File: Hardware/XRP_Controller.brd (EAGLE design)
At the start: 63.5 x 54 mm, 212 parts, among them J1 POWER_JACKPOWER_JACK_SLOT, J12 Vertical Qwiic Connector, J13 Vertical Qwiic Connector, J14 Vertical Qwiic Connector, J3 JST_6_PIN_VERTICAL, J4 JST_6_PIN_VERTICAL, J5 JST_6_PIN_VERTICAL, J6 JST_6_PIN_VERTICAL, J9 Vertical Qwiic Connector, Q3 20V/4.2A/52mΩ/1.4W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

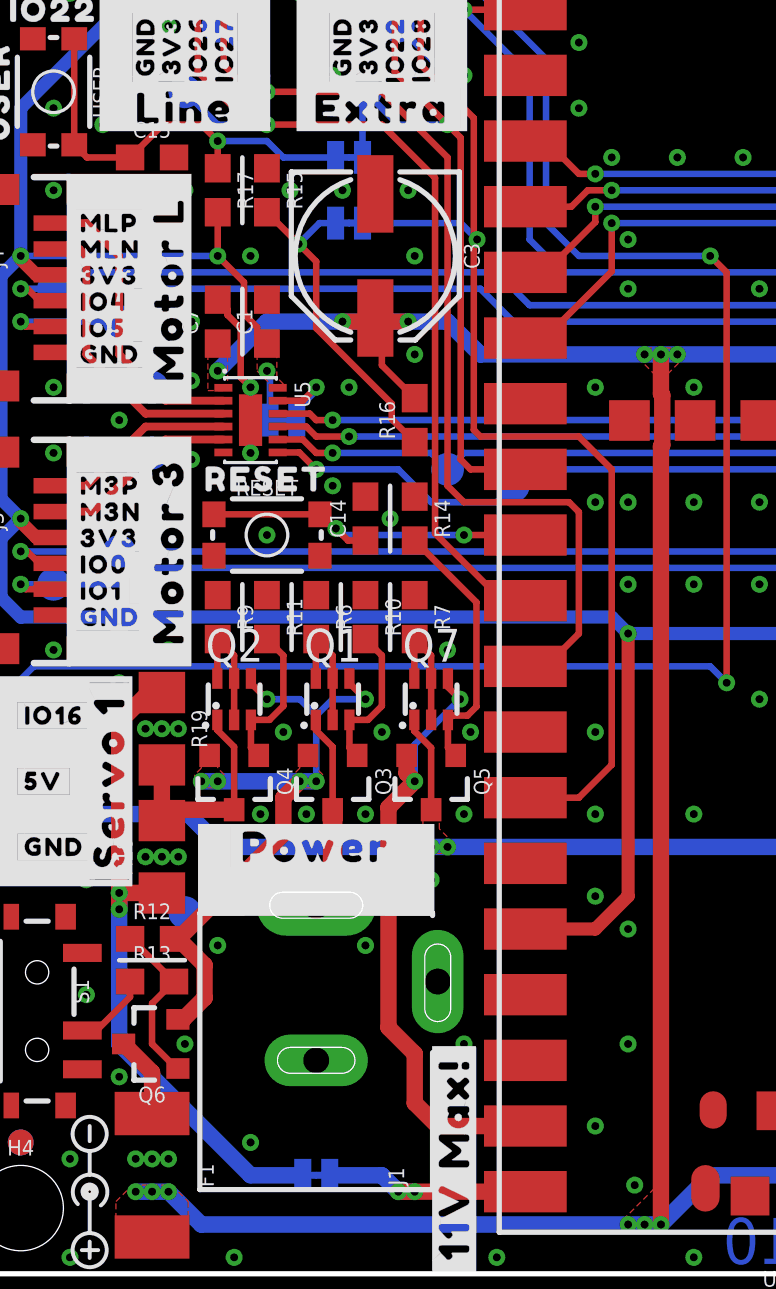
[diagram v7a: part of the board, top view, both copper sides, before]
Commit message: Minor tweaks
Nudge C3 to be on grid
Move MOT_3_EN via to not overlap with RESET silk
Nudge V_SYS trace and reduce width to get better GND pour
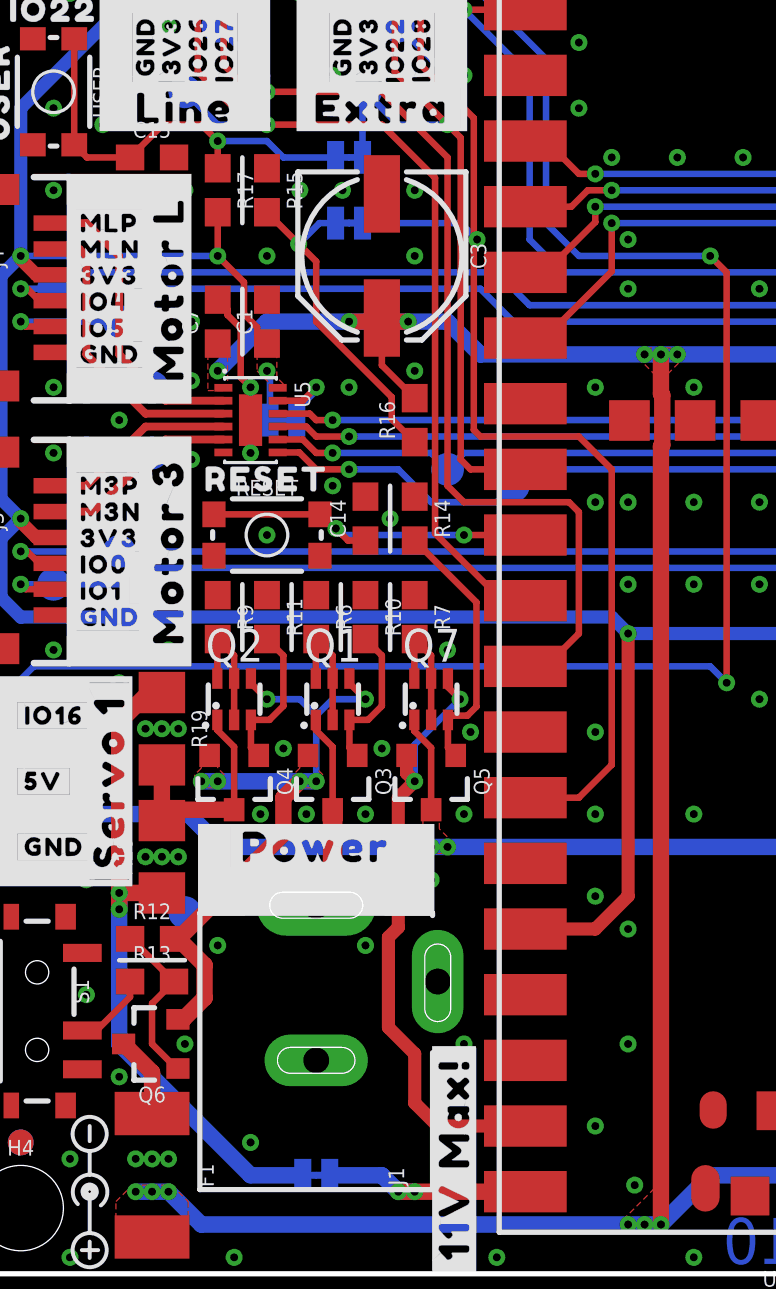
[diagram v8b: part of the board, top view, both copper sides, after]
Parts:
- moved C3 0.25 mm to (16.5, 39.4)
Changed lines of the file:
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@@
 <rectangle x1="41.783" y1="47.371" x2="42.037" y2="47.879" layer="41"/>
 <rectangle x1="39.243" y1="31.623" x2="39.624" y2="31.877" layer="41"/>
+<rectangle x1="17.653" y1="16.129" x2="17.907" y2="16.256" layer="41"/>
 </plain>
 <attributes>
@@
 <attribute name="VALUE" x="50.873" y="29.21" size="0.6096" layer="27" font="vector" ratio="20" rot="R270" align="top-center"/>
 </element>
-<element name="C3" library="SparkFun-Capacitors" package="PANASONIC_D" value="100uF" x="16.256" y="39.37" smashed="yes" rot="R270">
-<attribute name="NAME" x="19.685" y="39.37" size="0.6096" layer="25" font="vector" ratio="20" rot="R270" align="bottom-center"/>
-<attribute name="PN" value="EDH107M025A9HAA" x="16.256" y="39.37" size="1.778" layer="27" rot="R270" display="off"/>
-<attribute name="PROD_ID" value="CAP-17222" x="16.256" y="39.37" size="1.778" layer="27" font="vector" ratio="15" rot="R270" display="off"/>
-<attribute name="VALUE" value="100uF" x="12.827" y="39.37" size="0.6096" layer="27" font="vector" ratio="20" rot="R270" align="top-center"/>
+<element name="C3" library="SparkFun-Capacitors" package="PANASONIC_D" value="100uF" x="16.51" y="39.37" smashed="yes" rot="R270">
+<attribute name="NAME" x="19.939" y="39.37" size="0.6096" layer="25" font="vector" ratio="20" rot="R270" align="bottom-center"/>
+<attribute name="PN" value="EDH107M025A9HAA" x="16.51" y="39.37" size="1.778" layer="27" rot="R270" display="off"/>
+<attribute name="PROD_ID" value="CAP-17222" x="16.51" y="39.37" size="1.778" layer="27" font="vector" ratio="15" rot="R270" display="off"/>
+<attribute name="VALUE" value="100uF" x="13.081" y="39.37" size="0.6096" layer="27" font="vector" ratio="20" rot="R270" align="top-center"/>
 </element>
 <element name="C5" library="SparkFun-Capacitors" package="PANASONIC_D" value="100uF" x="50.8" y="39.37" smashed="yes" rot="R270">
@@
 <via x="36.195" y="3.429" extent="1-16" drill="0.3048"/>
 <via x="14.986" y="41.91" extent="1-16" drill="0.3048"/>
-<via x="17.526" y="41.91" extent="1-16" drill="0.3048"/>
-<via x="11.43" y="39.37" extent="1-16" drill="0.3048"/>
+<via x="17.78" y="41.91" extent="1-16" drill="0.3048"/>
+<via x="12.065" y="39.37" extent="1-16" drill="0.3048"/>
 <via x="9.144" y="36.83" extent="1-16" drill="0.3048"/>
 <via x="49.53" y="40.64" extent="1-16" drill="0.3048"/>
@@
 <via x="51.435" y="6.858" extent="1-16" drill="0.3048"/>
 <via x="43.815" y="4.445" extent="1-16" drill="0.3048"/>
-<via x="12.7" y="20.955" extent="1-16" drill="0.3048"/>
-<via x="16.51" y="20.955" extent="1-16" drill="0.3048"/>
+<via x="12.7" y="20.32" extent="1-16" drill="0.3048"/>
+<via x="16.51" y="20.32" extent="1-16" drill="0.3048"/>
 <via x="19.939" y="20.955" extent="1-16" drill="0.3048"/>
 <via x="7.366" y="21.082" extent="1-16" drill="0.3048"/>
@@
 <via x="0.635" y="44.45" extent="1-16" drill="0.3048"/>
 <via x="17.78" y="39.37" extent="1-16" drill="0.3048"/>
-<via x="17.78" y="35.56" extent="1-16" drill="0.3048"/>
+<via x="17.78" y="34.925" extent="1-16" drill="0.3048"/>
 <via x="9.144" y="34.544" extent="1-16" drill="0.3048"/>
 <via x="10.795" y="0.635" extent="1-16" drill="0.3048"/>
@@
 <via x="8.255" y="48.26" extent="1-16" drill="0.3048"/>
 <contactref element="R15" pad="1"/>
-<via x="12.954" y="41.91" extent="1-16" drill="0.3048"/>
+<via x="13.335" y="41.91" extent="1-16" drill="0.3048"/>
 <contactref element="USER" pad="1"/>
 <contactref element="USER" pad="2"/>
@@
 <wire x1="36.195" y1="31.115" x2="36.195" y2="20.828" width="0.254" layer="1"/>
 <via x="36.195" y="31.115" extent="1-16" drill="0.3048"/>
-<via x="13.97" y="31.115" extent="1-16" drill="0.3048"/>
+<via x="15.24" y="31.115" extent="1-16" drill="0.3048"/>
 <contactref element="U5" pad="7"/>
+<wire x1="15.24" y1="31.115" x2="13.97" y2="31.115" width="0.254" layer="1"/>
 <wire x1="13.97" y1="31.115" x2="13.315" y2="31.77" width="0.254" layer="1"/>
 <wire x1="13.315" y1="31.77" x2="12.48" y2="31.77" width="0.254" layer="1"/>
@@
 <wire x1="38.735" y1="15.24" x2="38.735" y2="18.288" width="0.254" layer="1"/>
 <wire x1="38.735" y1="18.288" x2="36.195" y2="20.828" width="0.254" layer="1"/>
-<wire x1="13.97" y1="31.115" x2="17.145" y2="31.115" width="0.254" layer="16"/>
+<wire x1="15.24" y1="31.115" x2="17.145" y2="31.115" width="0.254" layer="16"/>
 <wire x1="22.225" y1="31.115" x2="36.195" y2="31.115" width="0.254" layer="16"/>
 <wire x1="41.44" y1="13.335" x2="40.64" y2="13.335" width="0.254" layer="1"/>
@@
 </polygon>
 <wire x1="10.16" y1="34.925" x2="12.065" y2="36.83" width="0.635" layer="16"/>
-<wire x1="12.065" y1="36.83" x2="14.986" y2="36.83" width="0.635" layer="16"/>
-<via x="14.986" y="36.83" extent="1-16" drill="0.3048"/>
-<wire x1="14.986" y1="36.83" x2="17.526" y2="36.83" width="0.635" layer="16"/>
+<wire x1="12.065" y1="36.83" x2="15.24" y2="36.83" width="0.635" layer="16"/>
+<via x="15.24" y="36.83" extent="1-16" drill="0.3048"/>
+<wire x1="15.24" y1="36.83" x2="17.526" y2="36.83" width="0.635" layer="16"/>
 <via x="52.07" y="36.83" extent="1-16" drill="0.3048"/>
 <wire x1="17.526" y1="36.83" x2="19.05" y2="36.83" width="0.635" layer="16"/>
@@
 <wire x1="52.07" y1="36.83" x2="53.34" y2="35.56" width="0.635" layer="16"/>
 <wire x1="53.34" y1="35.56" x2="53.34" y2="31.115" width="0.635" layer="16"/>
-<wire x1="14.986" y1="36.83" x2="16.116" y2="36.83" width="0.635" layer="1"/>
-<wire x1="16.116" y1="36.83" x2="16.256" y2="36.97" width="0.508" layer="1"/>
-<wire x1="16.256" y1="36.97" x2="16.396" y2="36.83" width="0.508" layer="1"/>
-<wire x1="16.396" y1="36.83" x2="17.526" y2="36.83" width="0.635" layer="1"/>
+<wire x1="15.24" y1="36.83" x2="16.37" y2="36.83" width="0.635" layer="1"/>
+<wire x1="16.37" y1="36.83" x2="16.51" y2="36.97" width="0.508" layer="1"/>
+<wire x1="16.51" y1="36.97" x2="16.65" y2="36.83" width="0.508" layer="1"/>
+<wire x1="16.65" y1="36.83" x2="17.526" y2="36.83" width="0.635" layer="1"/>
 <via x="17.526" y="36.83" extent="1-16" drill="0.3048"/>
 <wire x1="50.8" y1="36.97" x2="50.94" y2="36.83" width="0.508" layer="1"/>
@@
 <contactref element="R16" pad="2"/>
 <wire x1="17.78" y1="33.87" x2="16.51" y2="35.14" width="0.254" layer="1"/>
-<wire x1="16.51" y1="36.716" x2="16.256" y2="36.97" width="0.254" layer="1"/>
-<wire x1="16.51" y1="36.716" x2="16.51" y2="35.14" width="0.254" layer="1"/>
+<wire x1="16.51" y1="36.97" x2="16.51" y2="35.14" width="0.254" layer="1"/>
 <via x="26.67" y="35.56" extent="1-16" drill="0.3048"/>
 <via x="27.94" y="35.56" extent="1-16" drill="0.3048"/>
@@
 <wire x1="19.065" y1="22.6926" x2="19.5326" y2="22.225" width="0.254" layer="1"/>
 <via x="19.5326" y="22.225" extent="1-16" drill="0.3048"/>
-<wire x1="17.465" y1="20.05" x2="17.465" y2="19.365" width="0.635" layer="1"/>
-<wire x1="17.465" y1="19.365" x2="17.78" y2="19.05" width="0.635" layer="1"/>
+<wire x1="17.465" y1="20.05" x2="17.465" y2="19.365" width="0.508" layer="1"/>
+<wire x1="17.465" y1="19.365" x2="17.78" y2="19.05" width="0.508" layer="1"/>
 <via x="17.78" y="19.05" extent="1-16" drill="0.3048"/>
 <wire x1="17.78" y1="19.05" x2="17.78" y2="20.4724" width="0.254" layer="16"/>
 <wire x1="17.78" y1="20.4724" x2="19.5326" y2="22.225" width="0.254" layer="16"/>
-<wire x1="17.78" y1="19.05" x2="16.764" y2="18.034" width="0.635" layer="1"/>
-<wire x1="16.764" y1="9.525" x2="16.764" y2="18.034" width="0.635" layer="1"/>
-<wire x1="17.78" y1="6.604" x2="18.669" y2="5.715" width="0.635" layer="1"/>
-<wire x1="22.06" y1="5.715" x2="18.669" y2="5.715" width="0.635" layer="1"/>
-<wire x1="16.764" y1="9.525" x2="17.78" y2="8.509" width="0.635" layer="1"/>
-<wire x1="17.78" y1="8.509" x2="17.78" y2="6.604" width="0.635" layer="1"/>
+<wire x1="17.78" y1="19.05" x2="17.145" y2="18.415" width="0.508" layer="1"/>
+<wire x1="16.764" y1="13.0175" x2="16.764" y2="9.525" width="0.508" layer="1"/>
+<wire x1="17.145" y1="18.415" x2="17.145" y2="13.3985" width="0.508" layer="1"/>
+<wire x1="17.78" y1="6.604" x2="18.669" y2="5.715" width="0.508" layer="1"/>
+<wire x1="22.06" y1="5.715" x2="18.669" y2="5.715" width="0.508" layer="1"/>
+<wire x1="16.764" y1="9.525" x2="17.78" y2="8.509" width="0.508" layer="1"/>
+<wire x1="17.78" y1="8.509" x2="17.78" y2="6.604" width="0.508" layer="1"/>
 <contactref element="U1" pad="39"/>
+<wire x1="17.145" y1="13.3985" x2="16.764" y2="13.0175" width="0.508" layer="1"/>
 </signal>
 <signal name="N$12">
@@
 <contactref element="R15" pad="2"/>
 <wire x1="17.78" y1="32.17" x2="16.891" y2="33.059" width="0.254" layer="1"/>
-<wire x1="16.891" y1="33.059" x2="16.891" y2="33.655" width="0.254" layer="1"/>
-<wire x1="16.891" y1="33.655" x2="13.97" y2="36.576" width="0.254" layer="1"/>
-<wire x1="13.97" y1="36.576" x2="13.97" y2="39.155" width="0.254" layer="1"/>
+<wire x1="16.891" y1="33.059" x2="16.891" y2="33.909" width="0.254" layer="1"/>
+<wire x1="16.891" y1="33.909" x2="13.97" y2="36.83" width="0.254" layer="1"/>
+<wire x1="13.97" y1="36.83" x2="13.97" y2="39.155" width="0.254" layer="1"/>
 <wire x1="12.065" y1="41.06" x2="13.291" y2="39.834" width="0.254" layer="1"/>
 <wire x1="13.291" y1="39.834" x2="13.97" y2="39.155" width="0.254" layer="1"/>
